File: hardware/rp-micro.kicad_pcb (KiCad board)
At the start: 2 copper layers, 17.8 x 33 mm, 44 parts, among them J1 USB_C_Receptacle_USB2.0, J2 Conn_01x12, J3 Conn_01x12, J4 Conn_01x05, SW1 BOOT, SW2 RESET, U1 RT9013-33GB, U2 W25Q64JVXGIQ, U3 RP2040, Y1 12MHz

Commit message: rev 1.1 completed
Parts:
- removed the LD1 at (132.8, 58.7)
- removed the R3 at (133.9, 60.5)
- removed kibuzzard-6360A6AE: G***, kibuzzard-6360A6AE
- added JP1: SolderJumper_3_Bridged12, Jumper:SolderJumper-3_P1.3mm_Bridged12_Pad1.0x1.5mm, B.Cu at (134.1, 66.0)
- added JP2: SolderJumper_3_Bridged12, Jumper:SolderJumper-3_P1.3mm_Bridged12_Pad1.0x1.5mm, B.Cu at (134.1, 68.6)
- added kibuzzard-637CA201: G***, kibuzzard-637CA201, B.Cu at (137.9, 81.1)
- J1: footprint rp-micro:USB_C_Receptacle_TYPE-C-31-M-12 -> rp-micro:USB Type-C Mid-Mount Receptacle 16P
- TP1: renamed from TP2; footprint TestPoint:TestPoint_Pad_D1.0mm -> TestPoint:TestPoint_Pad_D2.0mm
- TP2: renamed from TP3; footprint TestPoint:TestPoint_Pad_D1.0mm -> TestPoint:TestPoint_Pad_D2.0mm
- moved TP3 13.6 mm to (134.2, 84.6)
- moved LD1 13.5 mm to (134.9, 65.5)
- moved R9 13.0 mm to (134.2, 66.8), turned to 180 degrees
- moved R4 12.1 mm to (137.0, 84.2), turned to 90 degrees
- moved SW1 12.1 mm to (134.7, 85.1)
- moved SW2 12.1 mm to (144.7, 85.1)
- moved C15 5.77 mm to (145.5, 71.1), turned to -90 degrees
- moved D1 5.69 mm to (145.2, 66.3), turned to 90 degrees
- moved R5 5.62 mm to (134.0, 74.5), turned to 90 degrees
- moved R6 4.90 mm to (141.6, 66.9)
- moved R7 3.69 mm to (136.3, 66.8), turned to 180 degrees
- moved R8 3.61 mm to (144.9, 82.0), turned to 180 degrees
- moved C16 3.22 mm to (134.2, 67.8)
- moved F1 2.99 mm to (143.1, 66.4), turned to -90 degrees
- moved C3 2.97 mm to (137.0, 86.5), turned to 90 degrees
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- renumbered C6 to C1, C13 to C10, C14 to C11, C15 to C12, C16 to C13, C1 to C14, C2 to C15, C3 to C16, C9 to C2, C4 to C3, C5 to C4, C7 to C5, C10 to C6, C8 to C7, C11 to C8, C12 to C9, J4 to J3, J3 to J4, LD2 to LD1, R4 to R1, R5 to R2, R8 to R3, R7 to R4, R6 to R5, R1 to R6, R2 to R7, R9 to R8, R10 to R9, TP1 to TP3, U3 to U1, U1 to U3
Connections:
- net 22_SLCK renamed 22_SCLK
- net Net-(R4-Pad2) renamed /RPD+
- net Net-(R5-Pad2) renamed /RPD-
- net QSPI_0 renamed QSPI_D0
- net QSPI_1 renamed QSPI_D1
- net QSPI_2 renamed QSPI_D2
- net QSPI_3 renamed QSPI_D3
- D1 pad 2: VBUS -> +5V
- F1 pad 1: Net-(F1-Pad1) -> VBUS
- F1 pad 2: VBUS -> +5V
- J1 pad A4: Net-(F1-Pad1) -> VBUS
- J1 pad A9: Net-(F1-Pad1) -> VBUS
- J1 pad B4: Net-(F1-Pad1) -> VBUS
- J1 pad B9: Net-(F1-Pad1) -> VBUS
- J2 pad 3: GND -> Net-(J2-Pad3)
- J2 pad 4: GND -> Net-(J2-Pad4)
- J3 pad 1: 10 -> 12
- J3 pad 2: 11 -> 13
- J3 pad 3: 12 -> 14
- LD1 pad 1: GND -> Net-(LD1-Pad1)
- LD1 pad 2: Net-(LD2-Pad2) -> STATE_LED
- R9 pad 1: STATE_LED -> Net-(LD1-Pad1)
- R9 pad 2: Net-(LD2-Pad2) -> GND
- U1 pad 16: unconnected-(U3-Pad16) -> 13
- U1 pad 17: unconnected-(U3-Pad17) -> 14
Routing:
- net GND: track 65.1 -> 20.4 mm, vias 26 -> 36
- net +3V3: track 66.9 -> 50.1 mm, vias 7 -> 4
- net 10: track 8.71 -> 21.4 mm
- net QSPI_D1: track 16.2 -> 3.89 mm, vias 2 -> 0
- net Net-(F1-Pad1): track 11.1 -> 0.00 mm
- net STATE_LED: track 28.6 -> 18.2 mm, vias 4 -> 2
- net 14: track 0.00 -> 8.67 mm, vias 0 -> 1
- net Net-(J1-PadA5): track 11.4 -> 3.16 mm, vias 2 -> 0
- net 13: track 0.00 -> 7.77 mm, vias 0 -> 1
- net VBUS: track 2.08 -> 9.75 mm, vias 0 -> 2
- net 11: track 9.50 -> 16.8 mm
- net QSPI_D2: track 10.8 -> 3.79 mm
- net SWDIO: track 10.0 -> 4.52 mm
- net Net-(R3-Pad2): track 1.33 -> 5.62 mm
- net ~{RESET}: track 29.9 -> 26.5 mm, vias 2 -> 1
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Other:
- outline, holes or cut-outs redrawn
- board text added: "13"
- board text added: "14"

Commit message: Update PCBA files
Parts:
- C1, C10, C11, C12, C2, C5, C6, C8, C9: value 0.1uF -> 100nF
- C15: renamed from C16; value 0.1uF -> 100nF
- renumbered C15 to C16, JP1 to SB1, JP2 to SB2, TP3 to TP1, TP1 to TP2, TP2 to TP3
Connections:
- net Net-(J2-Pad3) renamed SB1_OUT
- net Net-(J2-Pad4) renamed SB2_OUT

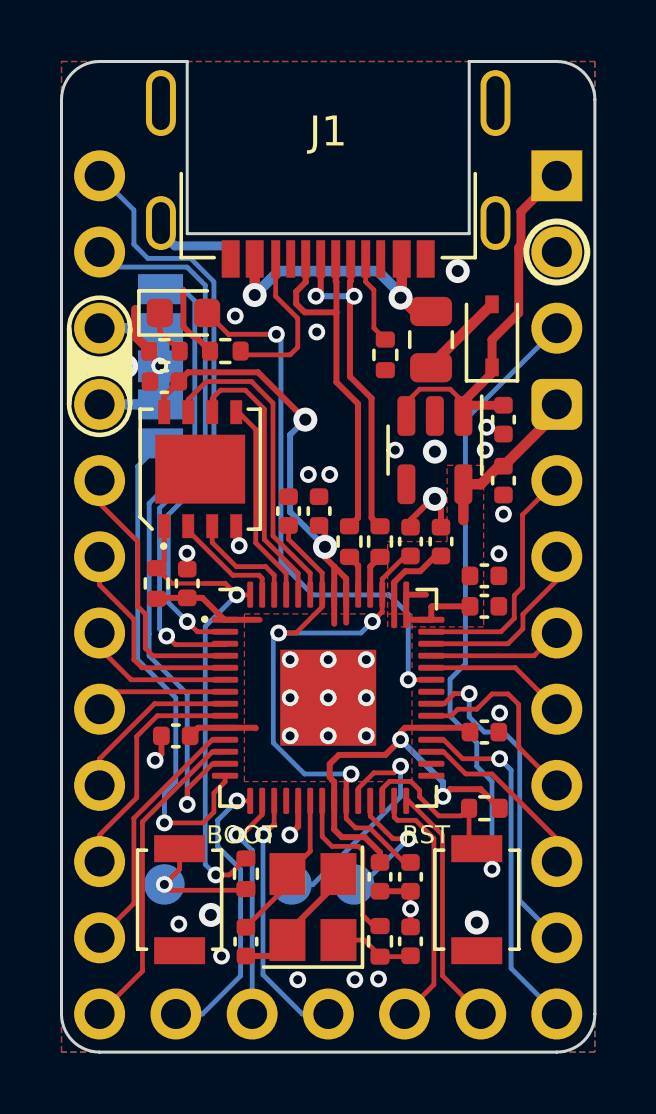
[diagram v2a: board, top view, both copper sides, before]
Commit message: Change D1 footprint to hand soldering version
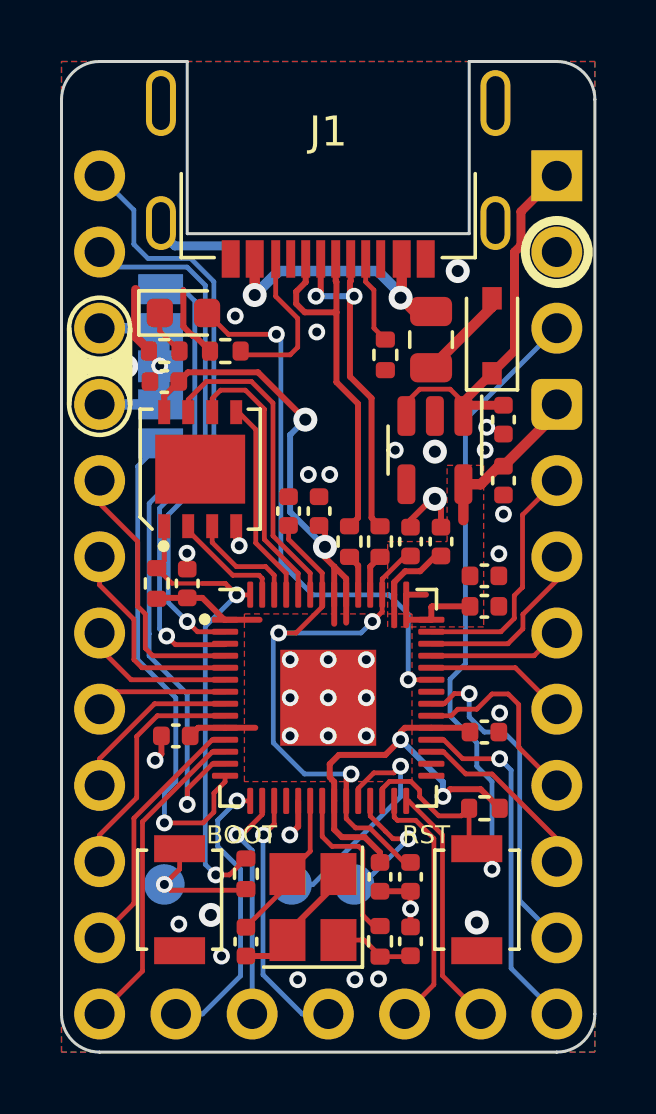
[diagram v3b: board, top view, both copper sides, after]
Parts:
- D1: footprint Diode_SMD:D_SOD-323 -> Diode_SMD:D_SOD-323_HandSoldering
- R9: value 330 -> 1k
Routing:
- net GND: track 20.4 -> 21.1 mm
